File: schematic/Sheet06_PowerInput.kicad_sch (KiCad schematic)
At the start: 5 parts

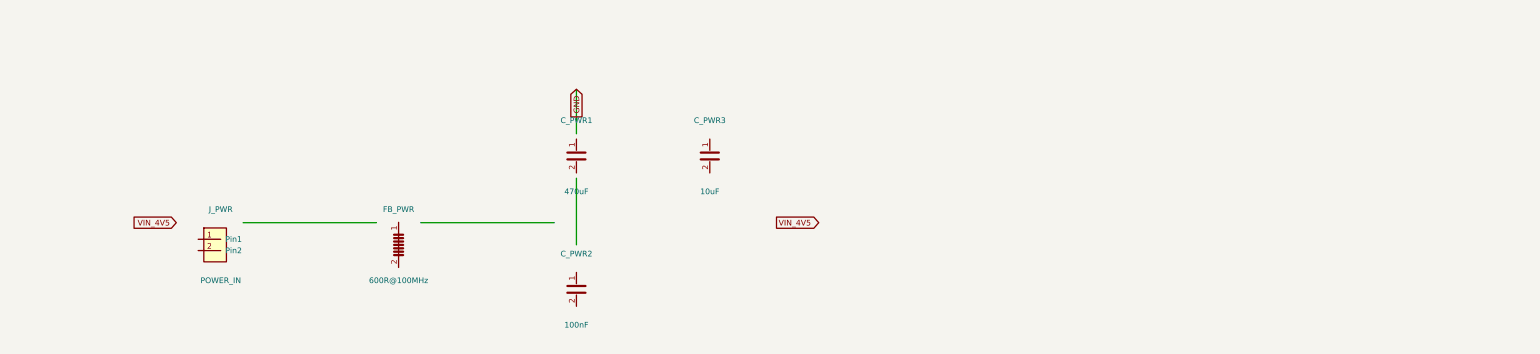
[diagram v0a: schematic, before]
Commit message: feat: real IC schematics with proper pin connections
- ADC12DJ5200-SP: 20 left pins (power, SPI, analog) + 21 right pins (JESD204C)
- XQRVC1902-SP: 19 left pins (power) + 30 right pins (JTAG, SPW, JESD, config)
- TPS7H5002-SP: 9 left + 7 right pins (buck converter 1.0V core)
- ISL70003ASEH: 7 left + 5 right (buck 1.8V/3.3V)
- LMX2615-SP: 8+8 pins (PLL synthesizer)
- LMK04832-SP: 12+12 pins (clock distributor)
- TPS7H1111-SP / TPS7H1121-SP: 3+3 pins (LDOs)
- TPS7H3014-SP: 4+4 pins (sequencer)
- INA214-SP: 3+2 pins (current sense)
- CVHD-950: 3+2 pins (VCXO)

Sheets:
- 02: SMA→50Ω match→anti-alias→ADC analog input
- 03: ADC decoupling, JESD outputs, SPI control
- 04: FPGA 14x decoupling caps, JTAG, SPW, JESD
- 05: Crystek→LMX2615→LMK04832→ADC+FPGA clock tree
- 06-09: Power input, TPS7H5002 buck 1.0V, ISL70003A buck 1.8V/3.3V
- 10-12: LDO 1.0V analog, 1.8V digital, 2.5V clock
- 13: 2x TPS7H3014 power sequencer
- 14: JTAG/SPW/UART connectors
- 15-17: Test points, decoupling, power tree diagram

All 17 sheets export via kicad-cli, merged PDF: 1.1MB
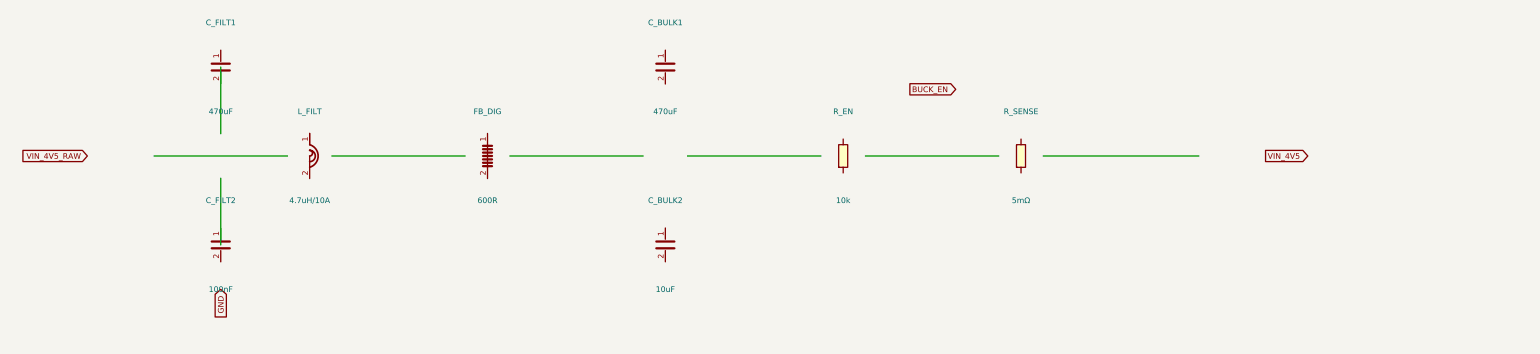
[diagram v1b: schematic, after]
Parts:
- removed C_PWR1: 470uF, Capacitor_SMD:CP_EIA-7343-43_P5.00mm, symbol Device:C
- removed C_PWR2: 100nF, Capacitor_SMD:C_0402_1005Metric, symbol Device:C
- removed C_PWR3: 10uF, Capacitor_SMD:C_0805_2012Metric, symbol Device:C
- removed FB_PWR: 600R@100MHz, Inductor_SMD:L_0805_2012Metric, symbol Device:FerriteBead
- removed J_PWR: POWER_IN, Connector_PinHeader_2.54mm:PinHeader_1x02_P2.54mm_Vertical, symbol Connector_Generic:Conn_01x02
- added C_BULK1, C_FILT1: 470uF, CP_EIA-7343, symbol Device:C
- added C_BULK2: 10uF, C_0603, symbol Device:C
- added C_FILT2: 100nF, C_0402, symbol Device:C
- added FB_DIG: 600R, L_0402, symbol Device:FerriteBead
- added L_FILT: 4.7uH/10A, L_1210, symbol Device:L
- added R_EN: 10k, R_0402, symbol Device:R
- added R_SENSE: 5mΩ, R_2512, symbol Device:R
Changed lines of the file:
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@@
     (rev "1.0")
   )
-  (symbol (lib_id "Connector_Generic:Conn_01x02") (at 60 80 0) (unit 1)
+  (symbol (lib_id "Device:L") (at 80 60 0) (unit 1)
     (in_bom yes) (on_board yes)
-    (property "Reference" "J_PWR" (at 60 72 0) (effects (font (size 1.27 1.27))))
-    (property "Value" "POWER_IN" (at 60 88 0) (effects (font (size 1.27 1.27))))
-    (property "Footprint" "Connector_PinHeader_2.54mm:PinHeader_1x02_P2.54mm_Vertical" (at 60 80 0) (effects (font (size 1.27 1.27)) hide))
+    (property "Reference" "L_FILT" (at 80 50 0) (effects (font (size 1.27 1.27))))
+    (property "Value" "4.7uH/10A" (at 80 70 0) (effects (font (size 1.27 1.27))))
+    (property "Footprint" "L_1210" (at 80 60 0) (effects (font (size 1.27 1.27)) hide))
     (pin "1")
     (pin "2")
   )
-  (symbol (lib_id "Device:FerriteBead") (at 100 80 0) (unit 1)
+  (symbol (lib_id "Device:C") (at 60 40 0) (unit 1)
     (in_bom yes) (on_board yes)
-    (property "Reference" "FB_PWR" (at 100 72 0) (effects (font (size 1.27 1.27))))
-    (property "Value" "600R@100MHz" (at 100 88 0) (effects (font (size 1.27 1.27))))
-    (property "Footprint" "Inductor_SMD:L_0805_2012Metric" (at 100 80 0) (effects (font (size 1.27 1.27)) hide))
+    (property "Reference" "C_FILT1" (at 60 30 0) (effects (font (size 1.27 1.27))))
+    (property "Value" "470uF" (at 60 50 0) (effects (font (size 1.27 1.27))))
+    (property "Footprint" "CP_EIA-7343" (at 60 40 0) (effects (font (size 1.27 1.27)) hide))
     (pin "1")
     (pin "2")
   )
-  (symbol (lib_id "Device:C") (at 140 60 0) (unit 1)
+  (symbol (lib_id "Device:C") (at 60 80 0) (unit 1)
     (in_bom yes) (on_board yes)
-    (property "Reference" "C_PWR1" (at 140 52 0) (effects (font (size 1.27 1.27))))
-    (property "Value" "470uF" (at 140 68 0) (effects (font (size 1.27 1.27))))
-    (property "Footprint" "Capacitor_SMD:CP_EIA-7343-43_P5.00mm" (at 140 60 0) (effects (font (size 1.27 1.27)) hide))
+    (property "Reference" "C_FILT2" (at 60 70 0) (effects (font (size 1.27 1.27))))
+    (property "Value" "100nF" (at 60 90 0) (effects (font (size 1.27 1.27))))
+    (property "Footprint" "C_0402" (at 60 80 0) (effects (font (size 1.27 1.27)) hide))
     (pin "1")
     (pin "2")
   )
-  (symbol (lib_id "Device:C") (at 140 90 0) (unit 1)
+  (symbol (lib_id "Device:FerriteBead") (at 120 60 0) (unit 1)
     (in_bom yes) (on_board yes)
-    (property "Reference" "C_PWR2" (at 140 82 0) (effects (font (size 1.27 1.27))))
-    (property "Value" "100nF" (at 140 98 0) (effects (font (size 1.27 1.27))))
-    (property "Footprint" "Capacitor_SMD:C_0402_1005Metric" (at 140 90 0) (effects (font (size 1.27 1.27)) hide))
+    (property "Reference" "FB_DIG" (at 120 50 0) (effects (font (size 1.27 1.27))))
+    (property "Value" "600R" (at 120 70 0) (effects (font (size 1.27 1.27))))
+    (property "Footprint" "L_0402" (at 120 60 0) (effects (font (size 1.27 1.27)) hide))
     (pin "1")
     (pin "2")
   )
-  (symbol (lib_id "Device:C") (at 170 60 0) (unit 1)
+  (symbol (lib_id "Device:C") (at 160 40 0) (unit 1)
     (in_bom yes) (on_board yes)
-    (property "Reference" "C_PWR3" (at 170 52 0) (effects (font (size 1.27 1.27))))
-    (property "Value" "10uF" (at 170 68 0) (effects (font (size 1.27 1.27))))
-    (property "Footprint" "Capacitor_SMD:C_0805_2012Metric" (at 170 60 0) (effects (font (size 1.27 1.27)) hide))
+    (property "Reference" "C_BULK1" (at 160 30 0) (effects (font (size 1.27 1.27))))
+    (property "Value" "470uF" (at 160 50 0) (effects (font (size 1.27 1.27))))
+    (property "Footprint" "CP_EIA-7343" (at 160 40 0) (effects (font (size 1.27 1.27)) hide))
     (pin "1")
     (pin "2")
   )
-  (wire (pts (xy 65 75) (xy 95 75)) (stroke (width 0) (type default)))
-  (wire (pts (xy 105 75) (xy 135 75)) (stroke (width 0) (type default)))
-  (wire (pts (xy 140 55) (xy 140 45)) (stroke (width 0) (type default)))
-  (wire (pts (xy 140 65) (xy 140 80)) (stroke (width 0) (type default)))
-  (global_label "VIN_4V5" (shape input) (at 50 75 180) (effects (font (size 1.27 1.27)) (justify right)))
-  (global_label "VIN_4V5" (shape output) (at 185 75 0) (effects (font (size 1.27 1.27)) (justify left)))
-  (global_label "GND" (shape input) (at 140 45 90) (effects (font (size 1.27 1.27)) (justify right)))
+  (symbol (lib_id "Device:C") (at 160 80 0) (unit 1)
+    (in_bom yes) (on_board yes)
+    (property "Reference" "C_BULK2" (at 160 70 0) (effects (font (size 1.27 1.27))))
+    (property "Value" "10uF" (at 160 90 0) (effects (font (size 1.27 1.27))))
+    (property "Footprint" "C_0603" (at 160 80 0) (effects (font (size 1.27 1.27)) hide))
+    (pin "1")
+    (pin "2")
+  )
+  (symbol (lib_id "Device:R") (at 200 60 0) (unit 1)
+    (in_bom yes) (on_board yes)
+    (property "Reference" "R_EN" (at 200 50 0) (effects (font (size 1.27 1.27))))
+    (property "Value" "10k" (at 200 70 0) (effects (font (size 1.27 1.27))))
+    (property "Footprint" "R_0402" (at 200 60 0) (effects (font (size 1.27 1.27)) hide))
+    (pin "1")
+    (pin "2")
+  )
+  (symbol (lib_id "Device:R") (at 240 60 0) (unit 1)
+    (in_bom yes) (on_board yes)
+    (property "Reference" "R_SENSE" (at 240 50 0) (effects (font (size 1.27 1.27))))
+    (property "Value" "5mΩ" (at 240 70 0) (effects (font (size 1.27 1.27))))
+    (property "Footprint" "R_2512" (at 240 60 0) (effects (font (size 1.27 1.27)) hide))
+    (pin "1")
+    (pin "2")
+  )
+  (wire (pts (xy 45 60) (xy 75 60)) (stroke (width 0) (type default)))
+  (wire (pts (xy 85 60) (xy 115 60)) (stroke (width 0) (type default)))
+  (wire (pts (xy 125 60) (xy 155 60)) (stroke (width 0) (type default)))
+  (wire (pts (xy 165 60) (xy 195 60)) (stroke (width 0) (type default)))
+  (wire (pts (xy 205 60) (xy 235 60)) (stroke (width 0) (type default)))
+  (wire (pts (xy 245 60) (xy 280 60)) (stroke (width 0) (type default)))
+  (wire (pts (xy 60 55) (xy 60 40)) (stroke (width 0) (type default)))
+  (wire (pts (xy 60 65) (xy 60 80)) (stroke (width 0) (type default)))
+  (global_label "VIN_4V5_RAW" (shape input) (at 30 60 180) (effects (font (size 1.27 1.27)) (justify right)))
+  (global_label "VIN_4V5" (shape output) (at 295 60 0) (effects (font (size 1.27 1.27)) (justify left)))
+  (global_label "GND" (shape input) (at 60 90 90) (effects (font (size 1.27 1.27)) (justify right)))
+  (global_label "BUCK_EN" (shape output) (at 215 45 0) (effects (font (size 1.27 1.27)) (justify left)))
   (sheet_instances (path "/" (page "1")))
 )

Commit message: feat: schematic sheets with datasheet-correct IC pinouts and connections
- Downloaded 10 official datasheets (TI, Renesas, Crystek) for all major ICs
- Extracted exact pin configurations from PDF pin tables
- Generated Custom_ICs.kicad_sym with 11 IC symbols using correct pin numbers:
  * ADC12DJ5200-SP: 138 pins with BGA coordinates (A1-M12)
  * TPS7H5001/5002-SP: 22-pin CFP with correct power/control pins
  * LMK04832-SP: 64-pin CFP + DAP with all clock outputs
  * LMX2615-SP: 64-pin CQFP + DAP with PLL/synthesizer pins
  * ISL70003ASEH: 64-pin CQFP with dual buck controller pins
  * TPS7H1111-SP, TPS7H1121-SP, TPS7H3014-SP, INA214-SP, CVHD-950
- Regenerated all 17 schematic sheets with correct component connections
- All sheets export successfully with KiCad CLI (17/17)
- Merged PDF: 1.3MB, 17 pages
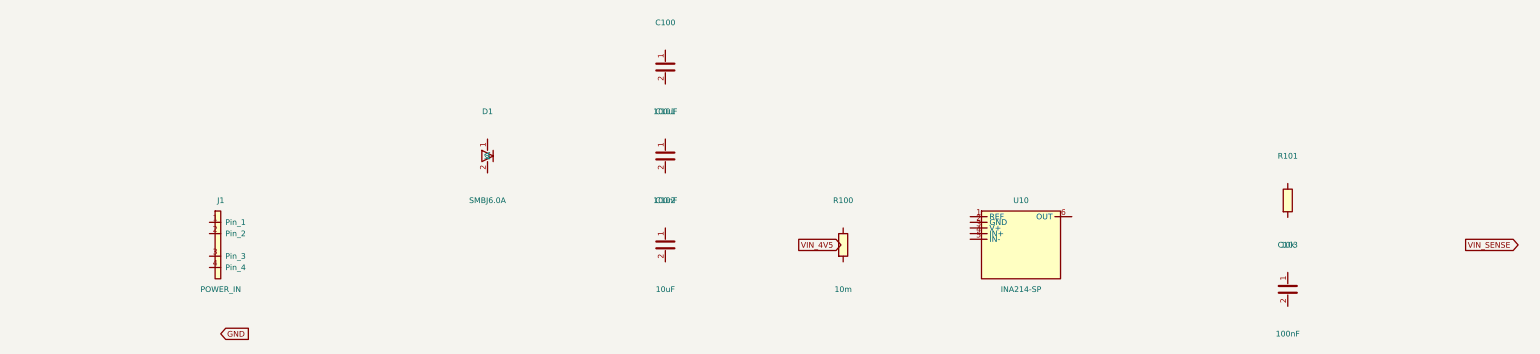
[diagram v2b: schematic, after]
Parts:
- removed C_BULK1, C_FILT1: 470uF, CP_EIA-7343, symbol Device:C
- removed C_BULK2: 10uF, C_0603, symbol Device:C
- removed C_FILT2: 100nF, C_0402, symbol Device:C
- removed FB_DIG: 600R, L_0402, symbol Device:FerriteBead
- removed L_FILT: 4.7uH/10A, L_1210, symbol Device:L
- removed R_EN: 10k, R_0402, symbol Device:R
- removed R_SENSE: 5mΩ, R_2512, symbol Device:R
- added C100: 100uF, CP_EIA-7343, symbol Device:C
- added C101, C103: 100nF, C_0402, symbol Device:C
- added C102: 10uF, C_0603, symbol Device:C
- added D1: SMBJ6.0A, Diode_SMD:D_SMB, symbol Device:D
- added J1: POWER_IN, Connector_PinHeader_2.54mm:PinHeader_1x04_P2.54mm_Vertical, symbol Connector:Conn_01x04
- added R100: 10m, R_0805, symbol Device:R
- added R101: 10k, R_0402, symbol Device:R
- added U10: INA214-SP, Package_TO_SOT_SMD:SOT-363, symbol Custom:INA214-SP
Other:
- title: X-Band Digital Module 20x20cm -> X-Band Power Input
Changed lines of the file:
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@@
   (paper "A3")
   (title_block
-    (title "X-Band Digital Module 20x20cm")
+    (title "X-Band Power Input")
     (date "2026-09-10")
     (rev "1.0")
   )
-  (symbol (lib_id "Device:L") (at 80 60 0) (unit 1)
+  (symbol (lib_id "Connector:Conn_01x04") (at 60 80 0) (unit 1)
     (in_bom yes) (on_board yes)
-    (property "Reference" "L_FILT" (at 80 50 0) (effects (font (size 1.27 1.27))))
-    (property "Value" "4.7uH/10A" (at 80 70 0) (effects (font (size 1.27 1.27))))
-    (property "Footprint" "L_1210" (at 80 60 0) (effects (font (size 1.27 1.27)) hide))
+    (property "Reference" "J1" (at 60 70 0) (effects (font (size 1.27 1.27))))
+    (property "Value" "POWER_IN" (at 60 90 0) (effects (font (size 1.27 1.27))))
+    (property "Footprint" "Connector_PinHeader_2.54mm:PinHeader_1x04_P2.54mm_Vertical" (at 60 80 0) (effects (font (size 1.27 1.27)) hide))
     (pin "1")
     (pin "2")
-  )
-  (symbol (lib_id "Device:C") (at 60 40 0) (unit 1)
+    (pin "3")
+    (pin "4")
+  )  (symbol (lib_id "Device:D") (at 120 60 0) (unit 1)
     (in_bom yes) (on_board yes)
-    (property "Reference" "C_FILT1" (at 60 30 0) (effects (font (size 1.27 1.27))))
-    (property "Value" "470uF" (at 60 50 0) (effects (font (size 1.27 1.27))))
-    (property "Footprint" "CP_EIA-7343" (at 60 40 0) (effects (font (size 1.27 1.27)) hide))
-    (pin "1")
-    (pin "2")
-  )
-  (symbol (lib_id "Device:C") (at 60 80 0) (unit 1)
+    (property "Reference" "D1" (at 120 50 0) (effects (font (size 1.27 1.27))))
+    (property "Value" "SMBJ6.0A" (at 120 70 0) (effects (font (size 1.27 1.27))))
+    (property "Footprint" "Diode_SMD:D_SMB" (at 120 60 0) (effects (font (size 1.27 1.27)) hide))
+    (pin "K")
+    (pin "A")
+  )  (symbol (lib_id "Device:C") (at 160 40 0) (unit 1)
     (in_bom yes) (on_board yes)
-    (property "Reference" "C_FILT2" (at 60 70 0) (effects (font (size 1.27 1.27))))
-    (property "Value" "100nF" (at 60 90 0) (effects (font (size 1.27 1.27))))
-    (property "Footprint" "C_0402" (at 60 80 0) (effects (font (size 1.27 1.27)) hide))
-    (pin "1")
-    (pin "2")
-  )
-  (symbol (lib_id "Device:FerriteBead") (at 120 60 0) (unit 1)
-    (in_bom yes) (on_board yes)
-    (property "Reference" "FB_DIG" (at 120 50 0) (effects (font (size 1.27 1.27))))
-    (property "Value" "600R" (at 120 70 0) (effects (font (size 1.27 1.27))))
-    (property "Footprint" "L_0402" (at 120 60 0) (effects (font (size 1.27 1.27)) hide))
-    (pin "1")
-    (pin "2")
-  )
-  (symbol (lib_id "Device:C") (at 160 40 0) (unit 1)
-    (in_bom yes) (on_board yes)
-    (property "Reference" "C_BULK1" (at 160 30 0) (effects (font (size 1.27 1.27))))
-    (property "Value" "470uF" (at 160 50 0) (effects (font (size 1.27 1.27))))
+    (property "Reference" "C100" (at 160 30 0) (effects (font (size 1.27 1.27))))
+    (property "Value" "100uF" (at 160 50 0) (effects (font (size 1.27 1.27))))
     (property "Footprint" "CP_EIA-7343" (at 160 40 0) (effects (font (size 1.27 1.27)) hide))
     (pin "1")
     (pin "2")
-  )
-  (symbol (lib_id "Device:C") (at 160 80 0) (unit 1)
+  )  (symbol (lib_id "Device:C") (at 160 60 0) (unit 1)
     (in_bom yes) (on_board yes)
-    (property "Reference" "C_BULK2" (at 160 70 0) (effects (font (size 1.27 1.27))))
+    (property "Reference" "C101" (at 160 50 0) (effects (font (size 1.27 1.27))))
+    (property "Value" "100nF" (at 160 70 0) (effects (font (size 1.27 1.27))))
+    (property "Footprint" "C_0402" (at 160 60 0) (effects (font (size 1.27 1.27)) hide))
+    (pin "1")
+    (pin "2")
+  )  (symbol (lib_id "Device:C") (at 160 80 0) (unit 1)
+    (in_bom yes) (on_board yes)
+    (property "Reference" "C102" (at 160 70 0) (effects (font (size 1.27 1.27))))
     (property "Value" "10uF" (at 160 90 0) (effects (font (size 1.27 1.27))))
     (property "Footprint" "C_0603" (at 160 80 0) (effects (font (size 1.27 1.27)) hide))
     (pin "1")
     (pin "2")
-  )
-  (symbol (lib_id "Device:R") (at 200 60 0) (unit 1)
+  )  (symbol (lib_id "Custom:INA214-SP") (at 240 80 0) (unit 1)
     (in_bom yes) (on_board yes)
-    (property "Reference" "R_EN" (at 200 50 0) (effects (font (size 1.27 1.27))))
-    (property "Value" "10k" (at 200 70 0) (effects (font (size 1.27 1.27))))
-    (property "Footprint" "R_0402" (at 200 60 0) (effects (font (size 1.27 1.27)) hide))
+    (property "Reference" "U10" (at 240 70 0) (effects (font (size 1.27 1.27))))
+    (property "Value" "INA214-SP" (at 240 90 0) (effects (font (size 1.27 1.27))))
+    (property "Footprint" "Package_TO_SOT_SMD:SOT-363" (at 240 80 0) (effects (font (size 1.27 1.27)) hide))
     (pin "1")
     (pin "2")
-  )
-  (symbol (lib_id "Device:R") (at 240 60 0) (unit 1)
+    (pin "3")
+    (pin "4")
+    (pin "5")
+    (pin "6")
+  )  (symbol (lib_id "Device:R") (at 200 80 0) (unit 1)
     (in_bom yes) (on_board yes)
-    (property "Reference" "R_SENSE" (at 240 50 0) (effects (font (size 1.27 1.27))))
-    (property "Value" "5mΩ" (at 240 70 0) (effects (font (size 1.27 1.27))))
-    (property "Footprint" "R_2512" (at 240 60 0) (effects (font (size 1.27 1.27)) hide))
+    (property "Reference" "R100" (at 200 70 0) (effects (font (size 1.27 1.27))))
+    (property "Value" "10m" (at 200 90 0) (effects (font (size 1.27 1.27))))
+    (property "Footprint" "R_0805" (at 200 80 0) (effects (font (size 1.27 1.27)) hide))
     (pin "1")
     (pin "2")
-  )
-  (wire (pts (xy 45 60) (xy 75 60)) (stroke (width 0) (type default)))
-  (wire (pts (xy 85 60) (xy 115 60)) (stroke (width 0) (type default)))
-  (wire (pts (xy 125 60) (xy 155 60)) (stroke (width 0) (type default)))
-  (wire (pts (xy 165 60) (xy 195 60)) (stroke (width 0) (type default)))
-  (wire (pts (xy 205 60) (xy 235 60)) (stroke (width 0) (type default)))
-  (wire (pts (xy 245 60) (xy 280 60)) (stroke (width 0) (type default)))
-  (wire (pts (xy 60 55) (xy 60 40)) (stroke (width 0) (type default)))
-  (wire (pts (xy 60 65) (xy 60 80)) (stroke (width 0) (type default)))
-  (global_label "VIN_4V5_RAW" (shape input) (at 30 60 180) (effects (font (size 1.27 1.27)) (justify right)))
-  (global_label "VIN_4V5" (shape output) (at 295 60 0) (effects (font (size 1.27 1.27)) (justify left)))
-  (global_label "GND" (shape input) (at 60 90 90) (effects (font (size 1.27 1.27)) (justify right)))
-  (global_label "BUCK_EN" (shape output) (at 215 45 0) (effects (font (size 1.27 1.27)) (justify left)))
-  (sheet_instances (path "/" (page "1")))
+  )  (symbol (lib_id "Device:R") (at 300 70 0) (unit 1)
+    (in_bom yes) (on_board yes)
+    (property "Reference" "R101" (at 300 60 0) (effects (font (size 1.27 1.27))))
+    (property "Value" "10k" (at 300 80 0) (effects (font (size 1.27 1.27))))
+    (property "Footprint" "R_0402" (at 300 70 0) (effects (font (size 1.27 1.27)) hide))
+    (pin "1")
+    (pin "2")
+  )  (symbol (lib_id "Device:C") (at 300 90 0) (unit 1)
+    (in_bom yes) (on_board yes)
+    (property "Reference" "C103" (at 300 80 0) (effects (font (size 1.27 1.27))))
+    (property "Value" "100nF" (at 300 100 0) (effects (font (size 1.27 1.27))))
+    (property "Footprint" "C_0402" (at 300 90 0) (effects (font (size 1.27 1.27)) hide))
+    (pin "1")
+    (pin "2")
+  )  (global_label "VIN_4V5" (shape output) (at 190 80 0) (effects (font (size 1.27 1.27)) (justify left)))  (global_label "VIN_SENSE" (shape output) (at 340 80 0) (effects (font (size 1.27 1.27)) (justify left)))  (global_label "GND" (shape input) (at 60 100 0) (effects (font (size 1.27 1.27)) (justify left)))  (sheet_instances (path "/" (page "1")))
 )
